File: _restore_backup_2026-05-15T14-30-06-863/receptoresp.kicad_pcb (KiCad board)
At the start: 2 copper layers, 48 x 59 mm, 7 parts

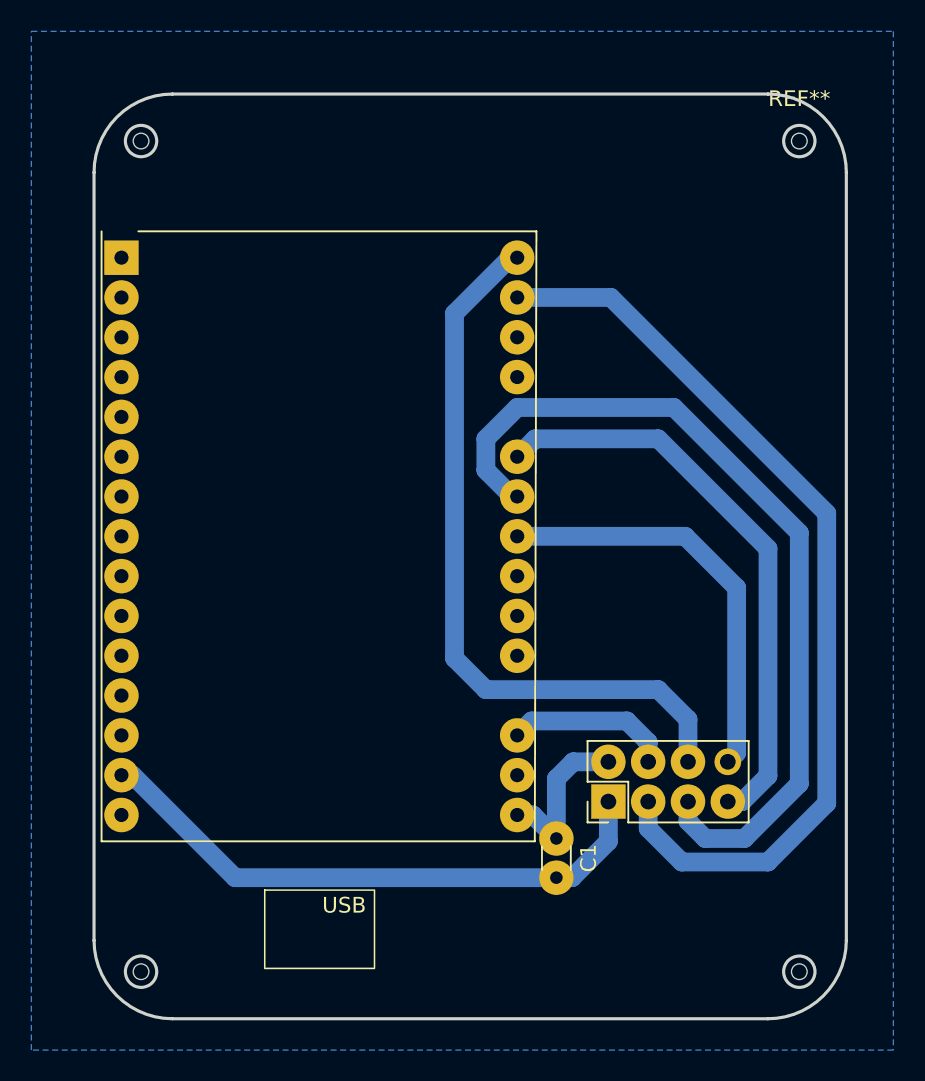
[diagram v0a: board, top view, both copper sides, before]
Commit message: capacitor polalizado 100uF
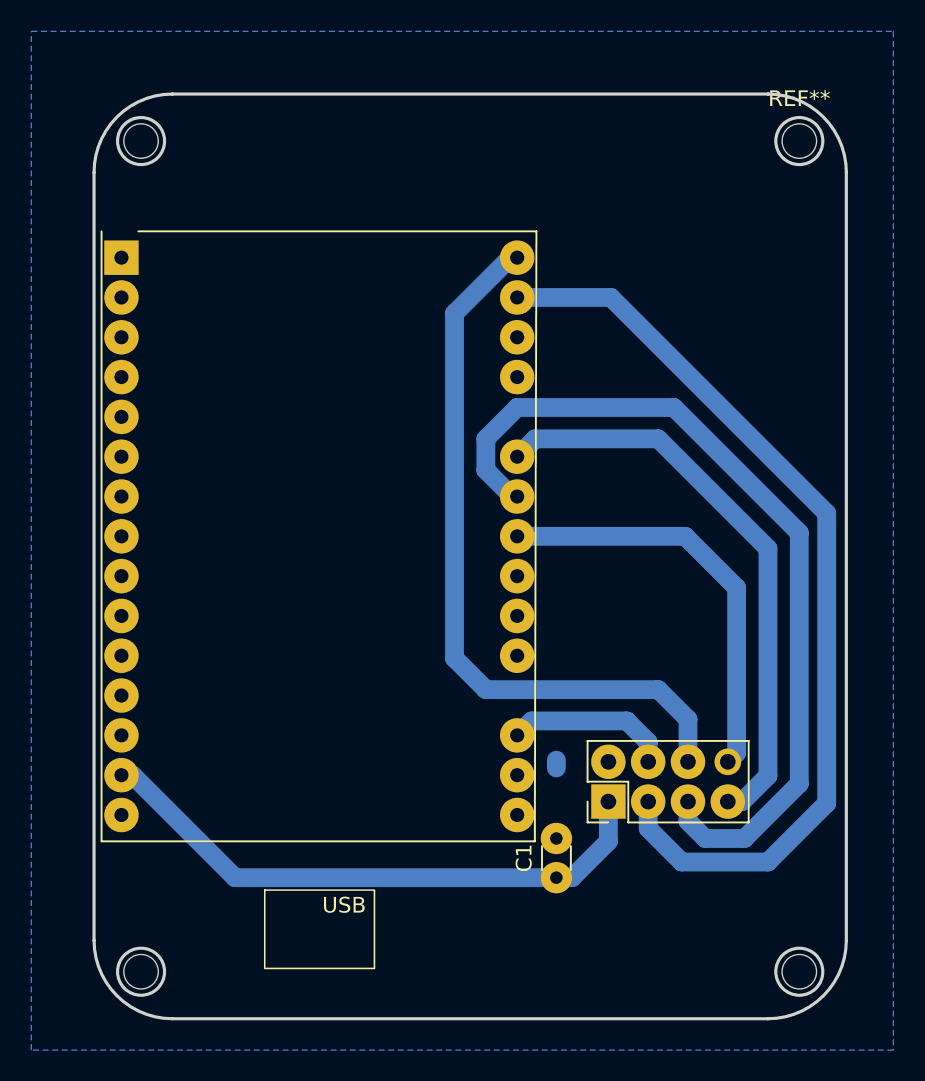
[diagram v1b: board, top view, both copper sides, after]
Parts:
- C1: value C_Polarized -> C
- moved C1 2.50 mm to (153.5, 104.0), turned to 90 degrees
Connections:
- C1 pad 2: Net-(NR1-GND) -> Net-(NR1-VCC)
- NR1 pad 2: Net-(E1-3V3) -> Net-(NR1-VCC)
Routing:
- net Net-(E1-3V3): track 10.7 -> 0.00 mm
- net Net-(NR1-VCC): track 0.00 -> 0.50 mm
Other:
- outline, holes or cut-outs redrawn
